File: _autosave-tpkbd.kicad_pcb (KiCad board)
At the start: 2 copper layers, 20 parts, among them CON1 AVR-ISP-6, J1 CONN_01X02, J2 CONN_01X01, J3 USB_OTG, J4 CONN_02X20, J5 CONN_01X04, J6 GS2, U1 ATMEGA8515-16AU, U2 AP111733, Y1 Crystal_GND24

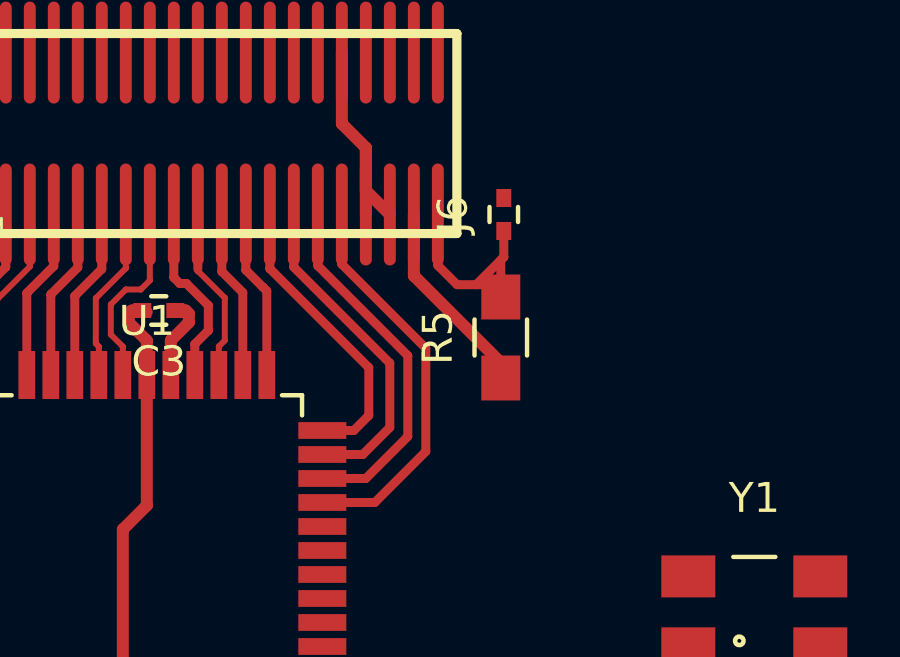
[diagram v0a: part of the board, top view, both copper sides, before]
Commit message: fixed tx14 conn
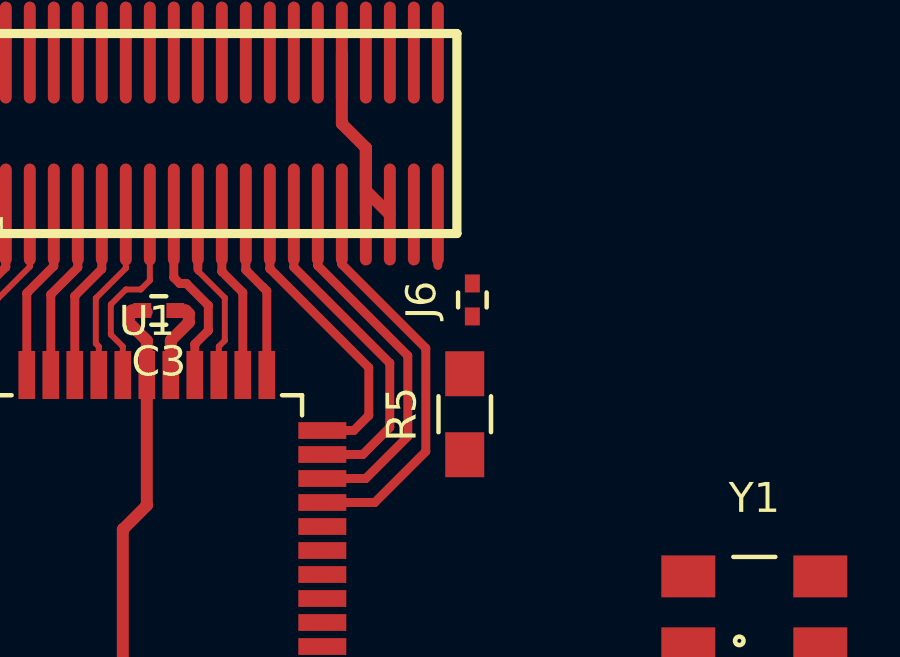
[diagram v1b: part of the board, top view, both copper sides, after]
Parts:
- moved J6 3.03 mm to (85.9, 41.1)
- moved R5 2.83 mm to (85.6, 45.0)
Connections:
- U1 pad 10: /tp_data -> /kb_id0
- U1 pad 11: /tp_ck -> /kb_id1
- U1 pad 27: /kb_id1 -> /tp_data
- U1 pad 29: /kb_id0 -> /tp_ck
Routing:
- net +5V: track 6.65 -> 0.00 mm
- net /tp_rst: track 7.20 -> 1.70 mm
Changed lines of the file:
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@@
   (general
     (links 83)
-    (no_connects 53)
+    (no_connects 56)
     (area 0 0 0 0)
     (thickness 1.6)
     (drawings 0)
-    (tracks 132)
+    (tracks 122)
     (zones 0)
     (modules 20)
@@
   )
   (module Resistors_SMD:R_0805_HandSoldering (layer F.Cu)
-    (at 86.8 42.4 90)
+    (at 85.598 44.958 90)
     (descr "Resistor SMD 0805, hand soldering")
     (tags "resistor 0805")
@@
       (net 44 "Net-(R3-Pad2)"))
     (pad 10 smd rect (at -5.85 3.2) (size 1.6 0.56) (layers F.Cu F.Paste F.Mask)
-      (net 39 /tp_data))
+      (net 35 /kb_id0))
     (pad 11 smd rect (at -5.85 4) (size 1.6 0.56) (layers F.Cu F.Paste F.Mask)
-      (net 40 /tp_ck))
+      (net 37 /kb_id1))
     (pad 12 smd rect (at -4 5.85 90) (size 1.6 0.56) (layers F.Cu F.Paste F.Mask)
       (net 13 /hotkey))
@@
       (net 38 /kb_id2))
     (pad 27 smd rect (at 5.85 0.8) (size 1.6 0.56) (layers F.Cu F.Paste F.Mask)
-      (net 37 /kb_id1))
+      (net 39 /tp_data))
     (pad 28 smd rect (at 5.85 0) (size 1.6 0.56) (layers F.Cu F.Paste F.Mask))
     (pad 29 smd rect (at 5.85 -0.8) (size 1.6 0.56) (layers F.Cu F.Paste F.Mask)
-      (net 35 /kb_id0))
+      (net 40 /tp_ck))
     (pad 30 smd rect (at 5.85 -1.6) (size 1.6 0.56) (layers F.Cu F.Paste F.Mask)
       (net 28 /A7))
@@
   )
   (module Capacitors_SMD:C_0402 (layer F.Cu)
-    (at 86.9 38.3 90)
+    (at 85.852 41.148 90)
     (descr "Capacitor SMD 0402, reflow soldering, AVX (see smccp.pdf)")
     (tags "capacitor 0402")
@@
     )
   )
-  (segment (start 82.3016 36.0736) (end 82.3016 37.4999) (width 0.4) (layer F.Cu) (net 2) (status 800000))
-  (segment (start 82.3016 37.4999) (end 83.1017 38.3) (width 0.4) (layer F.Cu) (net 2) (status C00000))
-  (segment (start 81.5015 32.9025) (end 81.5015 35.2735) (width 0.4) (layer F.Cu) (net 2) (status 400000))
-  (segment (start 82.3016 36.0736) (end 82.3016 38.3) (width 0.4) (layer F.Cu) (net 2) (status 800000))
+  (segment (start 82.3016 36.0736) (end 82.3016 37.4999) (width 0.4) (layer F.Cu) (net 2))
+  (segment (start 82.3016 37.4999) (end 83.1017 38.3) (width 0.4) (layer F.Cu) (net 2))
+  (segment (start 81.5015 32.9025) (end 81.5015 35.2735) (width 0.4) (layer F.Cu) (net 2))
+  (segment (start 82.3016 36.0736) (end 82.3016 38.3) (width 0.4) (layer F.Cu) (net 2))
   (segment (start 81.5015 35.2735) (end 82.3016 36.0736) (width 0.4) (layer F.Cu) (net 2))
   (segment (start 75 43.65) (end 75 42.5) (width 0.4) (layer F.Cu) (net 2))
@@
   (segment (start 76.4 41.9) (end 76.4 41.6) (width 0.4) (layer F.Cu) (net 4))
   (segment (start 75.8 42.5) (end 76.4 41.9) (width 0.4) (layer F.Cu) (net 4))
-  (segment (start 83.9018 38.3) (end 83.9018 40.3408) (width 0.4) (layer F.Cu) (net 5) (status 400000))
-  (segment (start 83.9018 40.3408) (end 86.8 43.239) (width 0.4) (layer F.Cu) (net 5) (status 800000))
-  (segment (start 86.8 43.239) (end 86.8 43.75) (width 0.4) (layer F.Cu) (net 5) (status C00000))
   (segment (start 68.16109 41.26109) (end 67.46109 41.96109) (width 0.3) (layer F.Cu) (net 6))
   (segment (start 70.3001 40.049898) (end 69.8 40.549998) (width 0.3) (layer F.Cu) (net 6))
@@
   (segment (start 71.9003 40.01771) (end 71.9003 38.3) (width 0.3) (layer F.Cu) (net 36))
   (segment (start 71 40.91801) (end 71.9003 40.01771) (width 0.3) (layer F.Cu) (net 36))
-  (segment (start 86.8 41.05) (end 86.8 39.819) (width 0.3) (layer F.Cu) (net 41) (status 400000))
-  (segment (start 86.8 39.819) (end 86.9 39.719) (width 0.3) (layer F.Cu) (net 41))
-  (segment (start 85.979 40.64) (end 86.39 40.64) (width 0.3) (layer F.Cu) (net 41) (status 800000))
-  (segment (start 84.7019 38.3) (end 84.7019 39.9979) (width 0.3) (layer F.Cu) (net 41) (status C00000))
-  (segment (start 84.7019 39.9979) (end 85.344 40.64) (width 0.3) (layer F.Cu) (net 41) (status 400000))
-  (segment (start 85.344 40.64) (end 85.979 40.64) (width 0.3) (layer F.Cu) (net 41))
-  (segment (start 85.979 40.64) (end 86.9 39.719) (width 0.3) (layer F.Cu) (net 41))
-  (segment (start 86.9 39.719) (end 86.9 38.85) (width 0.3) (layer F.Cu) (net 41) (status 800000))
+  (segment (start 84.7019 38.3) (end 84.7019 39.9979) (width 0.3) (layer F.Cu) (net 41))
   (segment (start 69.15 48.7) (end 67.3 48.7) (width 0.3) (layer F.Cu) (net 42))
   (segment (start 65.454 50.546) (end 59.182 50.546) (width 0.3) (layer F.Cu) (net 42))
   (segment (start 67.3 48.7) (end 65.454 50.546) (width 0.3) (layer F.Cu) (net 42))
-  (segment (start 69.15 51.1) (end 67.1 51.1) (width 0.3) (layer F.Cu) (net 43) (status 400000))
+  (segment (start 69.15 51.1) (end 67.1 51.1) (width 0.3) (layer F.Cu) (net 43))
   (segment (start 60.644 54.356) (end 57.658 54.356) (width 0.2) (layer F.Cu) (net 43))
   (segment (start 62.6 52.4) (end 60.644 54.356) (width 0.2) (layer F.Cu) (net 43))
